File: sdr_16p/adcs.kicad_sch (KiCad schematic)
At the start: 1 part, among them U3 ADAU1978xBCP

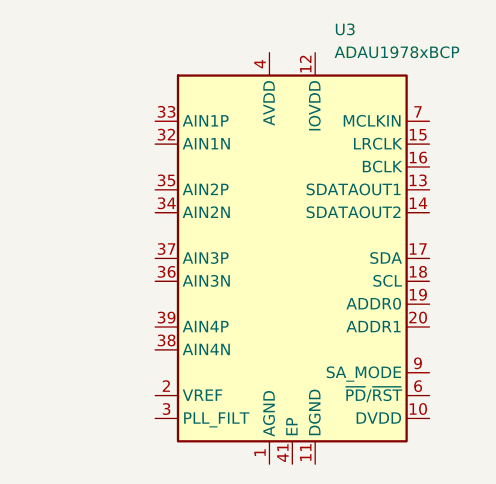
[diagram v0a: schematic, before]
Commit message: back to 16 phases
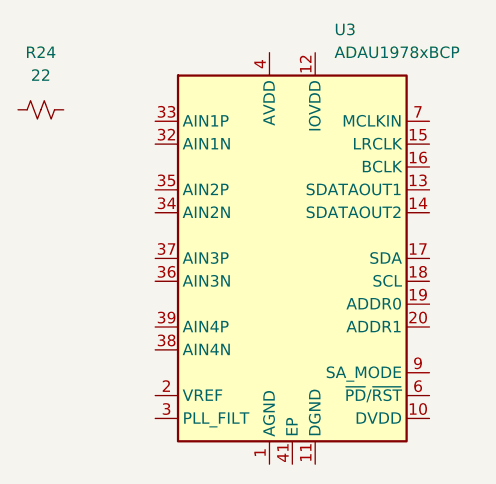
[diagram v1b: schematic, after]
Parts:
- added R24: 22, symbol Device:R_Small_US
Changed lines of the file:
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@@
+	)
+	(symbol
+		(lib_id "Device:R_Small_US")
+		(at 90.17 62.23 90)
+		(unit 1)
+		(exclude_from_sim no)
+		(in_bom yes)
+		(on_board yes)
+		(dnp no)
+		(fields_autoplaced yes)
+		(property "Reference" "R24"
+			(at 90.17 55.88 90)
+			(effects
+				(font
+					(size 1.27 1.27)
+				)
+			)
+		)
+		(property "Value" "22"
+			(at 90.17 58.42 90)
+			(effects
+				(font
+					(size 1.27 1.27)
+				)
+			)
+		)
+		(property "Footprint" ""
+			(at 90.17 62.23 0)
+			(effects
+				(font
+					(size 1.27 1.27)
+				)
+				(hide yes)
+			)
+		)
+		(property "Datasheet" "~"
+			(at 90.17 62.23 0)
+			(effects
+				(font
+					(size 1.27 1.27)
+				)
+				(hide yes)
+			)
+		)
+		(property "Description" "Resistor, small US symbol"
+			(at 90.17 62.23 0)
+			(effects
+				(font
+					(size 1.27 1.27)
+				)
+				(hide yes)
+			)
+		)
+		(pin "1"
+		)
+		(pin "2"
+		)
+		(instances
+			(project ""
+				(path "/fe42ca2f-2bb8-4d5a-9e84-807788ed632f/d1b276aa-cc76-4829-b01b-98095216e3ce"
+					(reference "R24")
+					(unit 1)
+				)
+			)
+		)
 	)
 	(symbol
